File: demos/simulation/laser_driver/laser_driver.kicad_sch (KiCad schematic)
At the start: 13 parts, among them Q1 fzt1049a, U1 AD8009

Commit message: Update some demos
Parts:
- U: renamed from V1; value pulse (check properties) -> (none)
- U: renamed from U1; value AD8009 -> (none)
- U: renamed from V2; value DC 10 -> (none)
- U: renamed from V3; value DC 10 -> (none)
- U: renamed from C2; value 1p -> (none)
- U: renamed from R5; value 2.5 -> (none)
- U: renamed from R1; value 220 -> (none)
- U: renamed from R3; value 220 -> (none)
- U: renamed from Q1; value fzt1049a -> (none)
- U: renamed from C1; value 1p -> (none)
- U: renamed from D1; value laser diode -> (none)
- U: renamed from R4; value 220 -> (none)
- U: renamed from R2; value 160 -> (none)

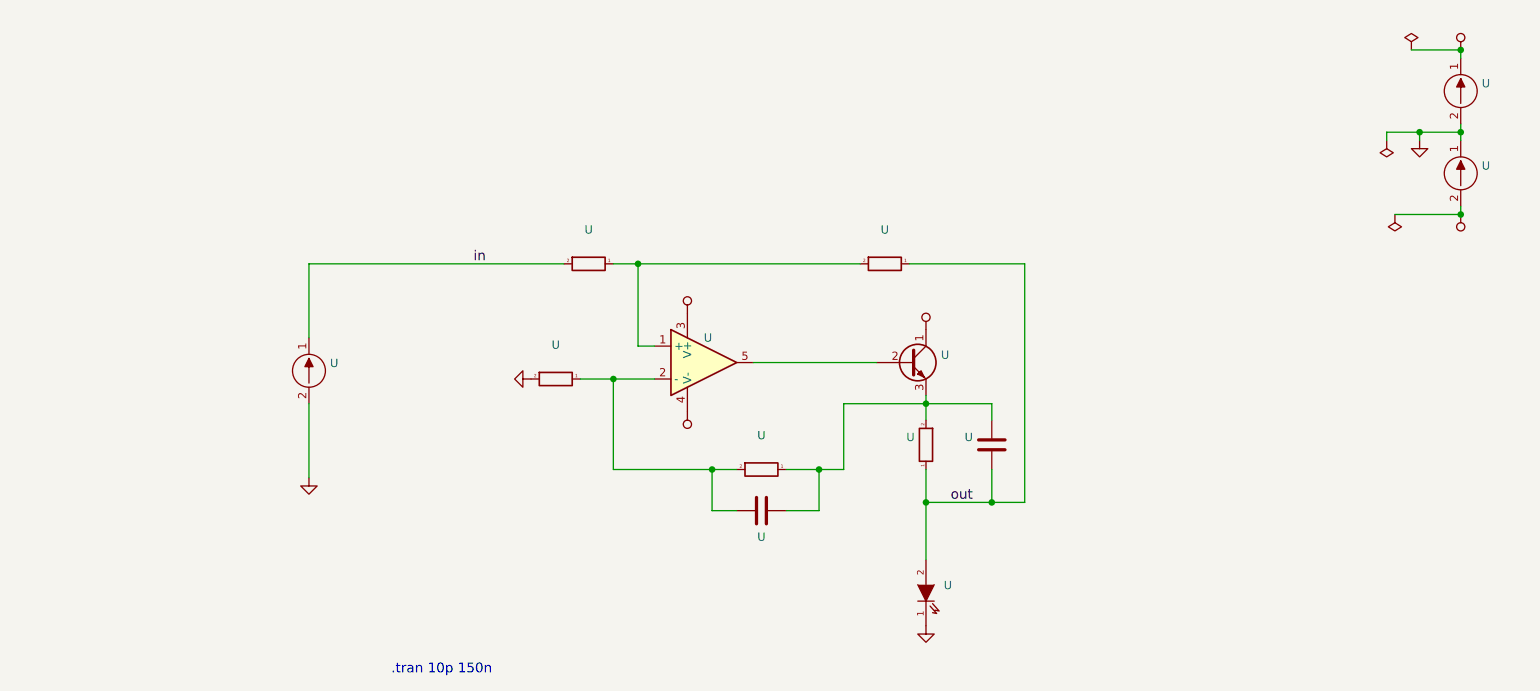
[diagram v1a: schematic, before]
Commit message: Update demos using latest file formats.
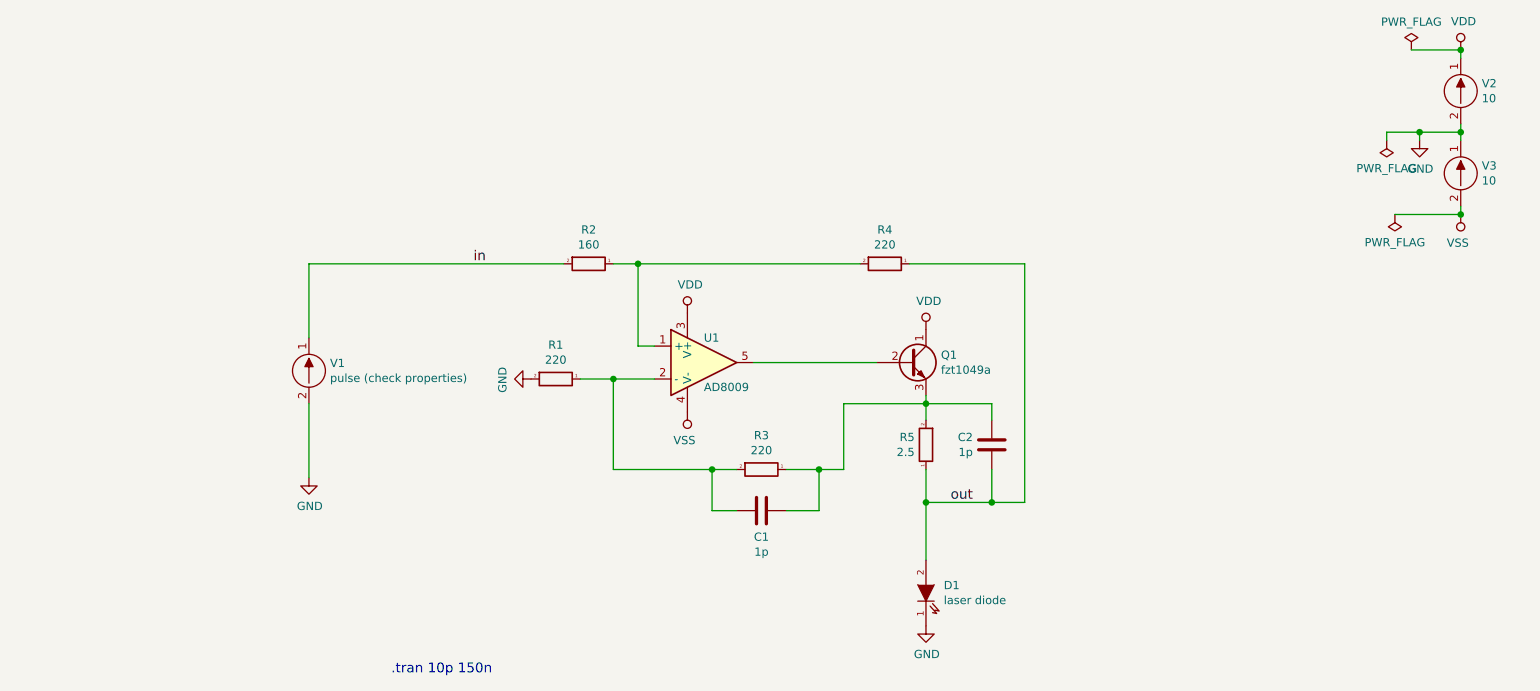
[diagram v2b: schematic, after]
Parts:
- C1, C2: renamed from U; value (none) -> 1p
- D1: renamed from U; value (none) -> laser diode; Spice_Lib_File laser.lib -> (none); Spice_Model laser -> (none); Spice_Netlist_Enabled Y -> (none); Spice_Node_Sequence 2 1 -> (none); Spice_Primitive D -> (none)
- Q1: renamed from U; value (none) -> fzt1049a; Spice_Lib_File fzt1049a.lib -> (none); Spice_Model fzt1049a -> (none); Spice_Netlist_Enabled Y -> (none); Spice_Primitive Q -> (none)
- R1, R3, R4: renamed from U; value (none) -> 220
- R2: renamed from U; value (none) -> 160
- R5: renamed from U; value (none) -> 2.5
- U1: renamed from U; value (none) -> AD8009; Spice_Lib_File ad8009.lib -> (none); Spice_Model ad8009 -> (none); Spice_Netlist_Enabled Y -> (none); Spice_Primitive X -> (none)
- V1: renamed from U; value (none) -> pulse (check properties); Spice_Model pulse(0 3 100n 1n 1n 20n 100n ) -> (none); Spice_Primitive V -> (none)
- V2, V3: renamed from U; value (none) -> 10; Spice_Node_Sequence 1 2 -> (none); Spice_Primitive V -> (none)

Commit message: Update laser_driver simulation example
This demo had some outdated symbols that don't look like the ones we
currently have in the upstream library.
Also some of the sim-parameters are now shown in the schematic to better
explain what is happening.
Hopefully that will make the example more accessible.

Resolves: https://gitlab.com/kicad/libraries/kicad-symbols/-/issues/3205
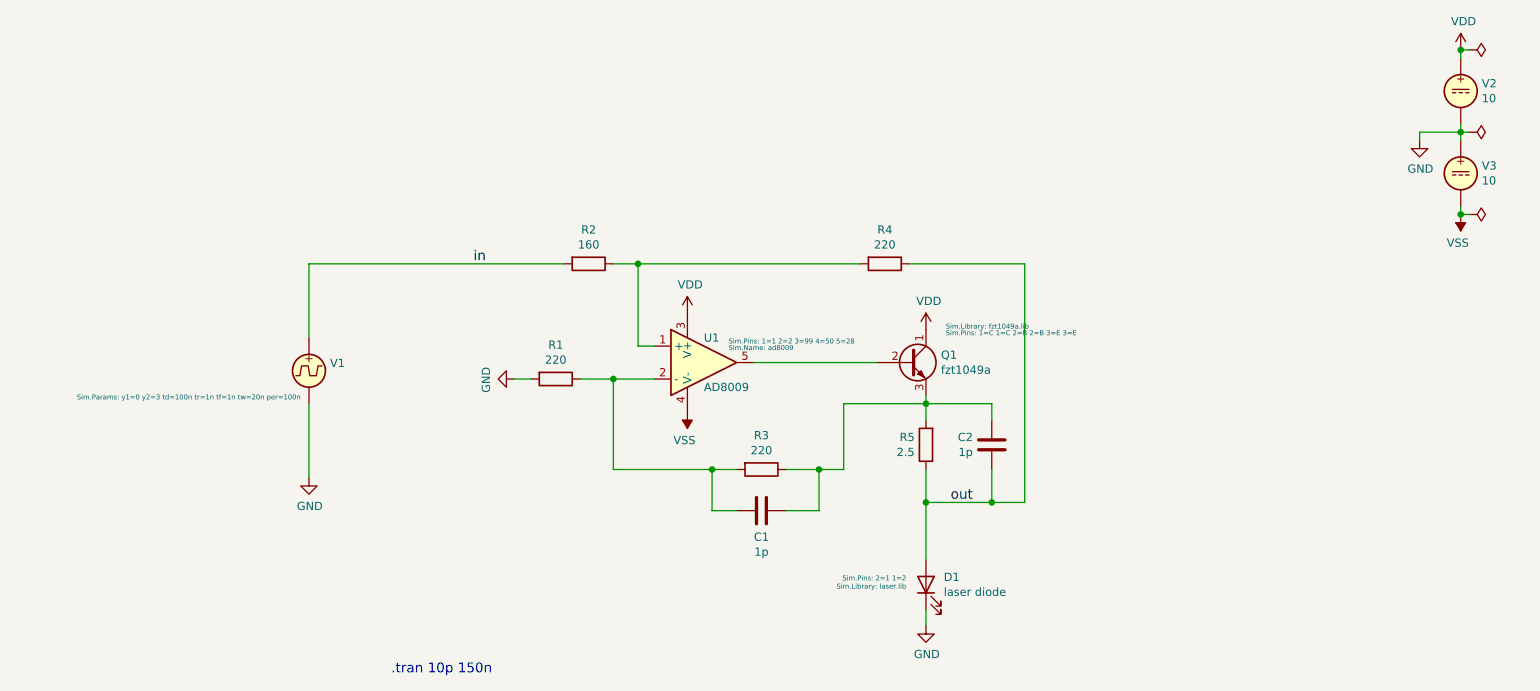
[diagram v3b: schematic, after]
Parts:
- Q1: Foo.Bar (none) -> 1337
- V1: symbol laser_driver_schlib:VSOURCE -> laser_driver_schlib:VPULSE
- V2, V3: symbol laser_driver_schlib:VSOURCE -> laser_driver_schlib:VDC
